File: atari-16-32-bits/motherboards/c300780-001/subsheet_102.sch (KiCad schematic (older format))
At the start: 0 parts

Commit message: done eprom
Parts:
- added C113, C114: 0.1uF, symbol Device:C
- added U102, U103: EPROM_32_PINS_DIP_PHY, Package_DIP:DIP-32_W15.24mm_LongPads, symbol eprom:EPROM_32_PINS_DIP_PHY
- added W102, W103, W104: SW_SPDT, symbol Switch:SW_SPDT
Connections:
- new net A1: U102.12 (A0), U103.12 (A0)
- new net A10: U102.26 (A9), U103.26 (A9)
- new net A11: U102.23 (A10), U103.23 (A10)
- new net A12: U102.25 (A11), U103.25 (A11)
- new net A13: U102.4 (A12), U103.4 (A12)
- new net A14: U102.28 (A13), U103.28 (A13)
- new net A15: U102.29 (A14), U103.29 (A14)
- new net A15_SELECT: U102.3 (A15), U103.3 (A15), W103.2 (B)
- new net A16: W103.3 (C)
- new net A16_SELECT: U102.2 (A16), U103.2 (A16), W104.2 (B)
- new net A17: W102.3 (C), W104.1 (A)
- new net A2: U102.11 (A1), U103.11 (A1)
- new net A3: U102.10 (A2), U103.10 (A2)
- new net A4: U102.9 (A3), U103.9 (A3)
- new net A5: U102.8 (A4), U103.8 (A4)
- new net A6: U102.7 (A5), U103.7 (A5)
- new net A7: U102.6 (A6), U103.6 (A6)
- new net A8: U102.5 (A7), U103.5 (A7)
- new net A9: U102.27 (A8), U103.27 (A8)
- new net D0: U103.13 (Q0)
- new net D1: U103.14 (Q1)
- new net D10: U102.15 (Q2)
- new net D11: U102.17 (Q3)
- new net D12: U102.18 (Q4)
- new net D13: U102.19 (Q5)
- new net D14: U102.20 (Q6)
- new net D15: U102.21 (Q7)
- new net D2: U103.15 (Q2)
- new net D3: U103.17 (Q3)
- new net D4: U103.18 (Q4)
- new net D5: U103.19 (Q5)
- new net D6: U103.20 (Q6)
- new net D7: U103.21 (Q7)
- new net D8: U102.13 (Q0)
- new net D9: U102.14 (Q1)
- new net GND: C113.2, C114.2, U102.16 (GND), U103.16 (GND), W102.1 (A), W104.3 (C)
- new net G_SELECT: U102.24 (~G~), U103.24 (~G~), W102.2 (B)
- new net VCC: C113.1, C114.1, U102.1 (Vpp), U102.30 (NC), U102.31 (~P~), U102.32 (Vcc), U103.1 (Vpp), U103.30 (NC), U103.31 (~P~), U103.32 (Vcc), W103.1 (A)
- new net XROM2: U102.22 (~E~), U103.22 (~E~)
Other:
- note added: "Part Type\n\n27256\n27512\n571001/27C1000/531000\n27010/571000/27C1001"
- note added: "ROM jumper settings"
- note added: "W102\n\nDon't care\n2 and 3\n2 and 3\n1 and 2"
- note added: "W103\n\n1 and 2\n2 and 3\n2 and 3\n2 and 3"
- note added: "W104\n\nN/C\nN/C\n2 and 3\n1 and 2"

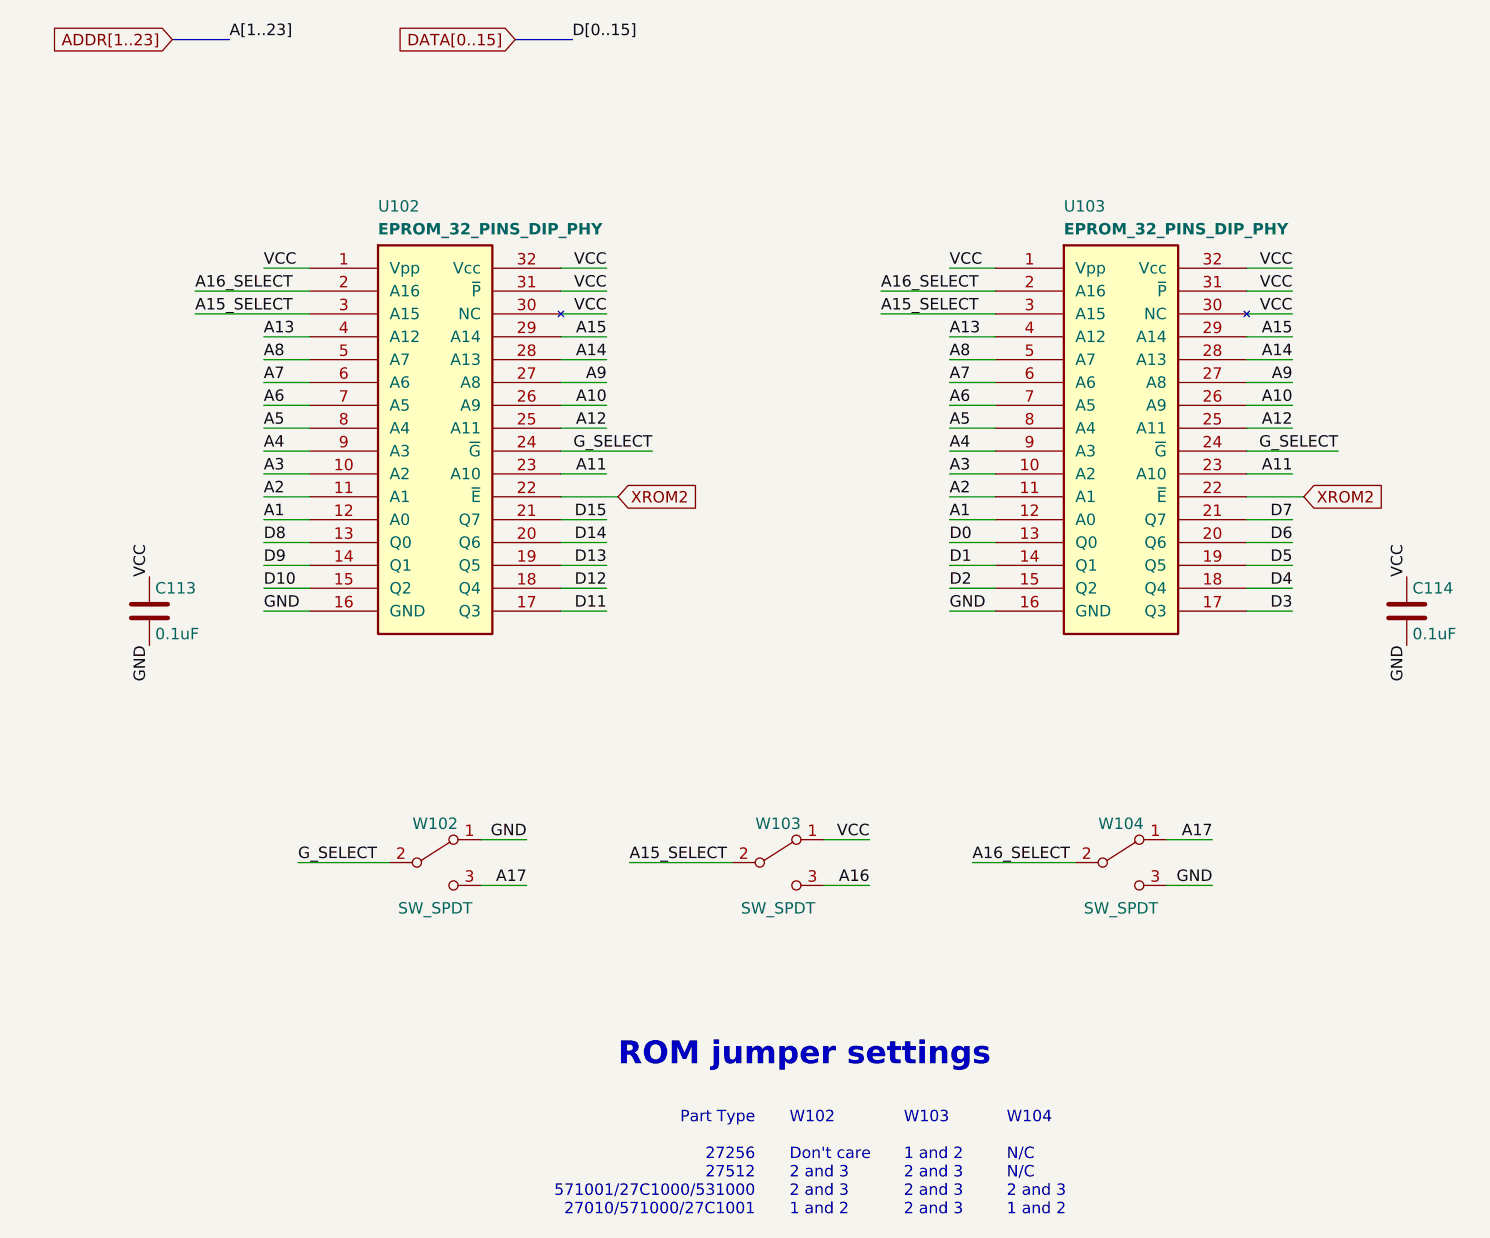
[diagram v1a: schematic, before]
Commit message: reorganized sheets
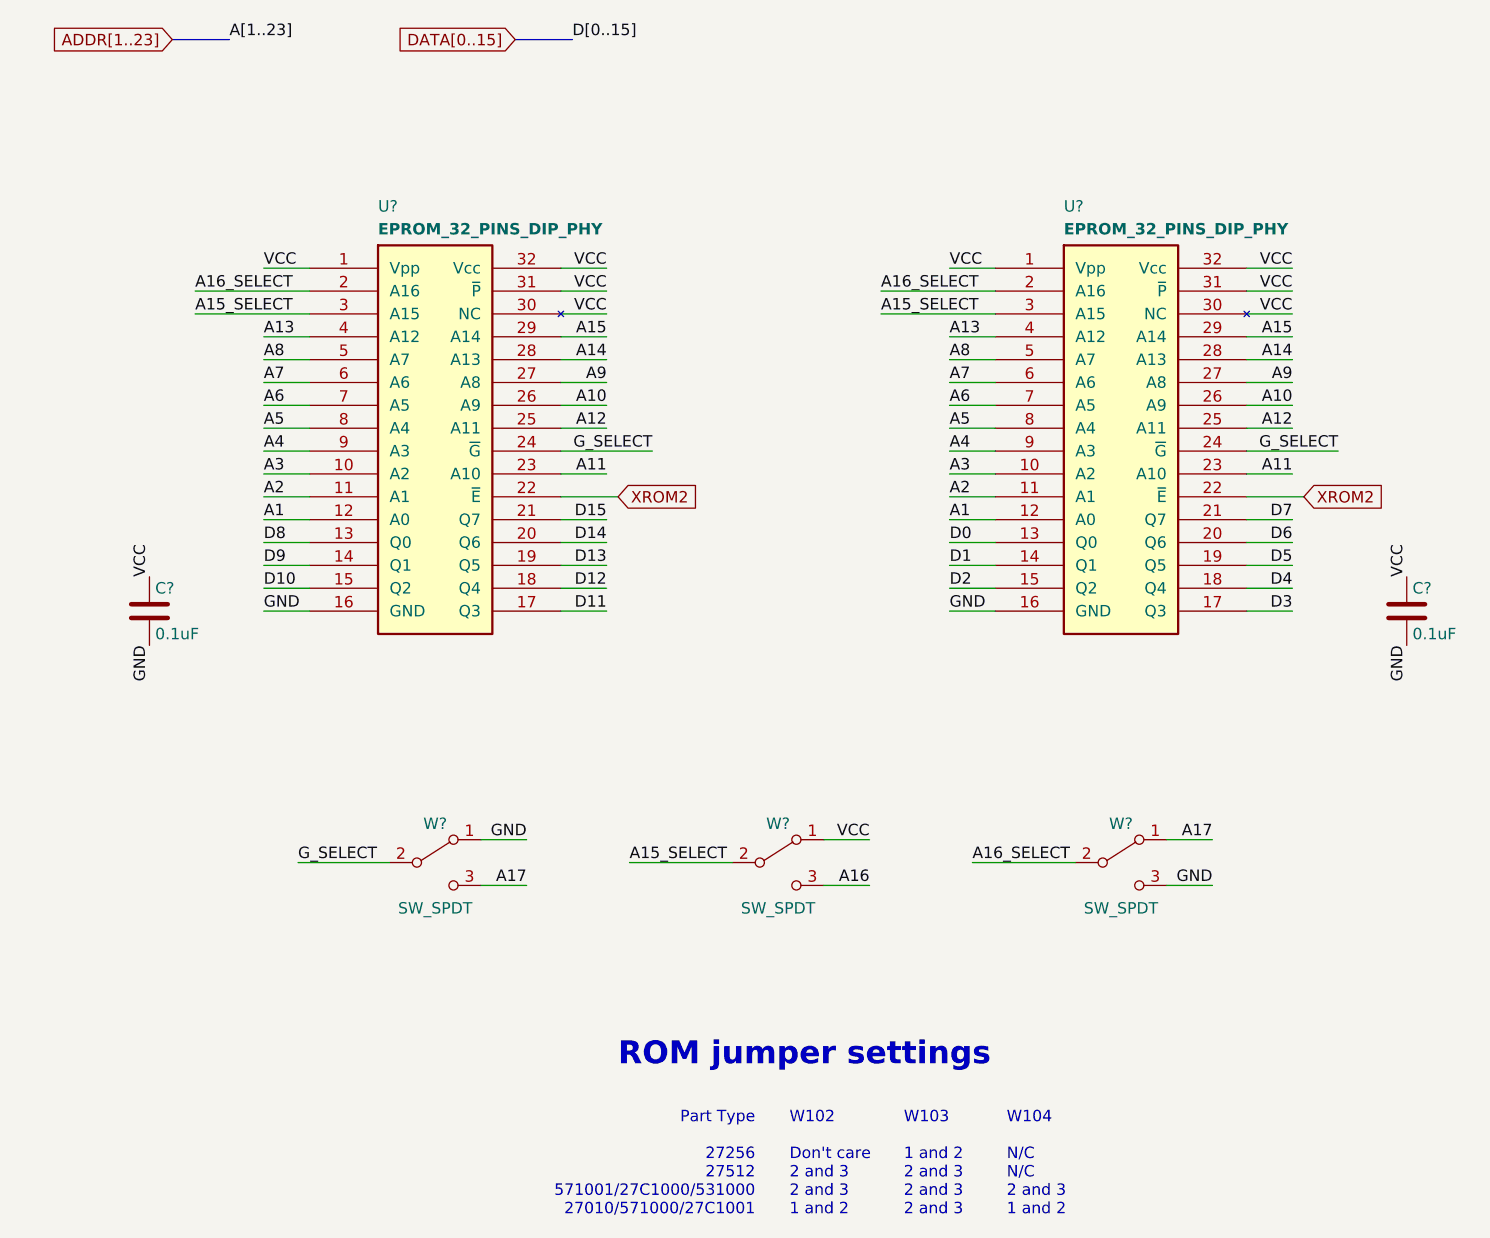
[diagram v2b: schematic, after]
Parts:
- renumbered U102 to U?, U103 to U?, W102 to W?, W103 to W?, W104 to W?
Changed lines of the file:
@@
 $Descr A4 8268 11693 portrait
 encoding utf-8
-Sheet 5 14
+Sheet 9 8
 Title ""
 Date ""
@@
 D[0..15]
 $Comp
-L eprom:EPROM_32_PINS_DIP_PHY U102
+L eprom:EPROM_32_PINS_DIP_PHY U?
 U 1 1 607E83E6
 P 2650 2750
-F 0 "U102" H 2400 3800 50  0000 L TNN
+F 0 "U?" H 2400 3800 50  0000 L TNN
 F 1 "EPROM_32_PINS_DIP_PHY" H 2400 3700 50  0000 L TNB
 F 2 "Package_DIP:DIP-32_W15.24mm_LongPads" H 2400 3900 50  0001 L TNN
@@
 $EndComp
 $Comp
-L eprom:EPROM_32_PINS_DIP_PHY U103
+L eprom:EPROM_32_PINS_DIP_PHY U?
 U 1 1 607E97A4
 P 5650 2750
-F 0 "U103" H 5400 3800 50  0000 L TNN
+F 0 "U?" H 5400 3800 50  0000 L TNN
 F 1 "EPROM_32_PINS_DIP_PHY" H 5400 3700 50  0000 L TNB
 F 2 "Package_DIP:DIP-32_W15.24mm_LongPads" H 5400 3900 50  0001 L TNN
@@
 AR Path="/60786F27/6078774E/6083D581" Ref="C?"  Part="1"
 AR Path="/60786F27/60787615/6083D581" Ref="C113"  Part="1"
-F 0 "C113" H 1425 3600 50  0000 L CNN
+AR Path="/6089D0BC/6083D581" Ref="C?"  Part="1"
+F 0 "C?" H 1425 3600 50  0000 L CNN
 F 1 "0.1uF" H 1425 3400 50  0000 L CNN
 F 2 "" H 1438 3350 50  0001 C CNN
@@
 AR Path="/60786F27/6078774E/6083D587" Ref="C?"  Part="1"
 AR Path="/60786F27/60787615/6083D587" Ref="C114"  Part="1"
-F 0 "C114" H 6925 3600 50  0000 L CNN
+AR Path="/6089D0BC/6083D587" Ref="C?"  Part="1"
+F 0 "C?" H 6925 3600 50  0000 L CNN
 F 1 "0.1uF" H 6925 3400 50  0000 L CNN
 F 2 "" H 6938 3350 50  0001 C CNN
@@
 VCC
 $Comp
-L Switch:SW_SPDT W102
+L Switch:SW_SPDT W?
 U 1 1 60856AEC
 P 2650 4600
-F 0 "W102" H 2650 4770 50  0000 C CNN
+F 0 "W?" H 2650 4770 50  0000 C CNN
 F 1 "SW_SPDT" H 2650 4400 50  0000 C CNN
 F 2 "" H 2650 4600 50  0001 C CNN
@@
 $EndComp
 $Comp
-L Switch:SW_SPDT W103
+L Switch:SW_SPDT W?
 U 1 1 608575E4
 P 4150 4600
-F 0 "W103" H 4150 4770 50  0000 C CNN
+F 0 "W?" H 4150 4770 50  0000 C CNN
 F 1 "SW_SPDT" H 4150 4400 50  0000 C CNN
 F 2 "" H 4150 4600 50  0001 C CNN
@@
 $EndComp
 $Comp
-L Switch:SW_SPDT W104
+L Switch:SW_SPDT W?
 U 1 1 608589B0
 P 5650 4600
-F 0 "W104" H 5650 4770 50  0000 C CNN
+F 0 "W?" H 5650 4770 50  0000 C CNN
 F 1 "SW_SPDT" H 5650 4400 50  0000 C CNN
 F 2 "" H 5650 4600 50  0001 C CNN

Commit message: re-annotate component following move of subsheets in schematics
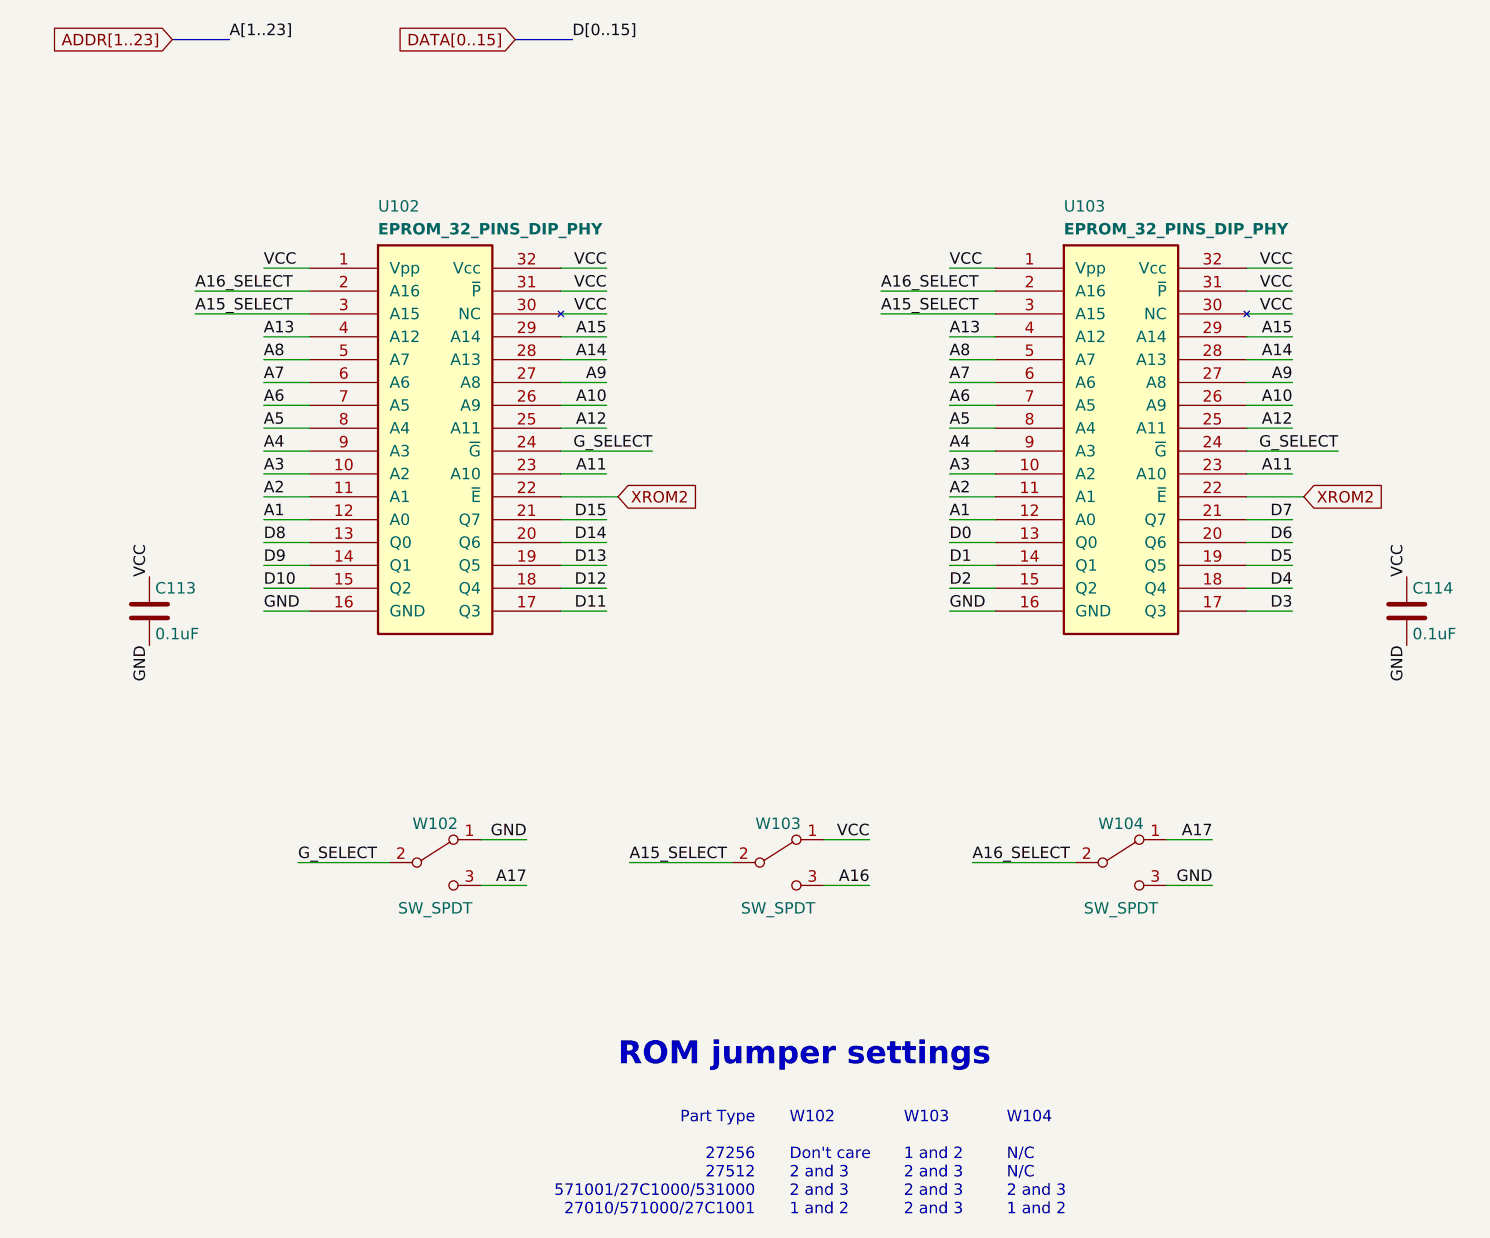
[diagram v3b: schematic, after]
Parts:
- gave numbers to parts that had none: 5
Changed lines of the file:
@@
 $Descr A4 8268 11693 portrait
 encoding utf-8
-Sheet 9 8
+Sheet 3 9
 Title ""
 Date ""
@@
 D[0..15]
 $Comp
-L eprom:EPROM_32_PINS_DIP_PHY U?
+L eprom:EPROM_32_PINS_DIP_PHY U102
 U 1 1 607E83E6
 P 2650 2750
-F 0 "U?" H 2400 3800 50  0000 L TNN
+F 0 "U102" H 2400 3800 50  0000 L TNN
 F 1 "EPROM_32_PINS_DIP_PHY" H 2400 3700 50  0000 L TNB
 F 2 "Package_DIP:DIP-32_W15.24mm_LongPads" H 2400 3900 50  0001 L TNN
@@
 $EndComp
 $Comp
-L eprom:EPROM_32_PINS_DIP_PHY U?
+L eprom:EPROM_32_PINS_DIP_PHY U103
 U 1 1 607E97A4
 P 5650 2750
-F 0 "U?" H 5400 3800 50  0000 L TNN
+F 0 "U103" H 5400 3800 50  0000 L TNN
 F 1 "EPROM_32_PINS_DIP_PHY" H 5400 3700 50  0000 L TNB
 F 2 "Package_DIP:DIP-32_W15.24mm_LongPads" H 5400 3900 50  0001 L TNN
@@
 AR Path="/60786F27/6078774E/6083D581" Ref="C?"  Part="1"
 AR Path="/60786F27/60787615/6083D581" Ref="C113"  Part="1"
-AR Path="/6089D0BC/6083D581" Ref="C?"  Part="1"
-F 0 "C?" H 1425 3600 50  0000 L CNN
+AR Path="/6089D0BC/6083D581" Ref="C113"  Part="1"
+F 0 "C113" H 1425 3600 50  0000 L CNN
 F 1 "0.1uF" H 1425 3400 50  0000 L CNN
 F 2 "" H 1438 3350 50  0001 C CNN
@@
 AR Path="/60786F27/6078774E/6083D587" Ref="C?"  Part="1"
 AR Path="/60786F27/60787615/6083D587" Ref="C114"  Part="1"
-AR Path="/6089D0BC/6083D587" Ref="C?"  Part="1"
-F 0 "C?" H 6925 3600 50  0000 L CNN
+AR Path="/6089D0BC/6083D587" Ref="C114"  Part="1"
+F 0 "C114" H 6925 3600 50  0000 L CNN
 F 1 "0.1uF" H 6925 3400 50  0000 L CNN
 F 2 "" H 6938 3350 50  0001 C CNN
@@
 VCC
 $Comp
-L Switch:SW_SPDT W?
+L Switch:SW_SPDT W102
 U 1 1 60856AEC
 P 2650 4600
-F 0 "W?" H 2650 4770 50  0000 C CNN
+F 0 "W102" H 2650 4770 50  0000 C CNN
 F 1 "SW_SPDT" H 2650 4400 50  0000 C CNN
 F 2 "" H 2650 4600 50  0001 C CNN
@@
 $EndComp
 $Comp
-L Switch:SW_SPDT W?
+L Switch:SW_SPDT W103
 U 1 1 608575E4
 P 4150 4600
-F 0 "W?" H 4150 4770 50  0000 C CNN
+F 0 "W103" H 4150 4770 50  0000 C CNN
 F 1 "SW_SPDT" H 4150 4400 50  0000 C CNN
 F 2 "" H 4150 4600 50  0001 C CNN
@@
 $EndComp
 $Comp
-L Switch:SW_SPDT W?
+L Switch:SW_SPDT W104
 U 1 1 608589B0
 P 5650 4600
-F 0 "W?" H 5650 4770 50  0000 C CNN
+F 0 "W104" H 5650 4770 50  0000 C CNN
 F 1 "SW_SPDT" H 5650 4400 50  0000 C CNN
 F 2 "" H 5650 4600 50  0001 C CNN
